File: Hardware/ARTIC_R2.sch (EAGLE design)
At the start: 103 parts, among them J1 U.FL, J2 THING_PLUS, Q1 20V/4.2A/52mΩ/1.4W, U1 32M SPI Flash, U2 1.8V/100mA, U3 ARTIC_R2, U4 RFPA0133, U5 AS179-92LF, U6 DUAL-OPTOISOLATOR_SOIC8, X1 CRYSTAL-TCXO-26MHZ

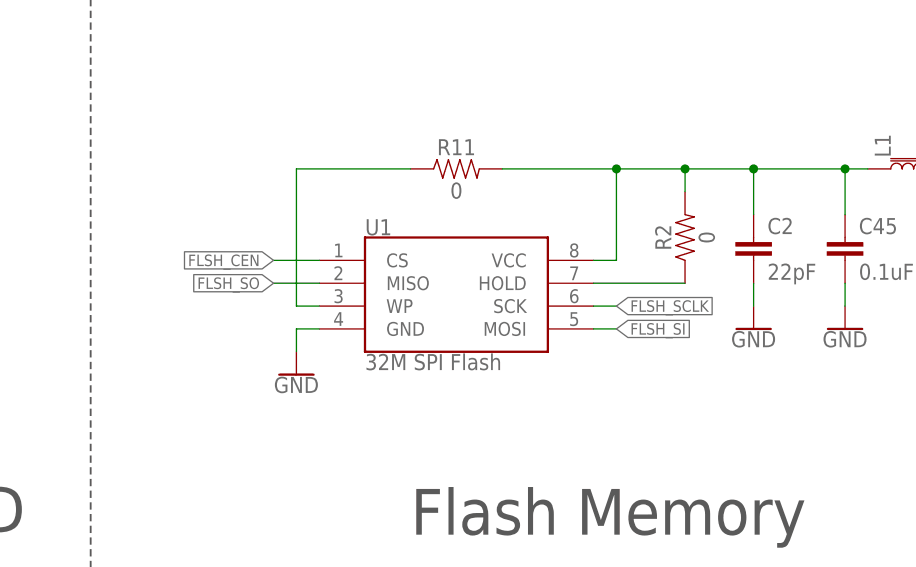
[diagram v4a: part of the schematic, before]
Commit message: Updated the flash memory
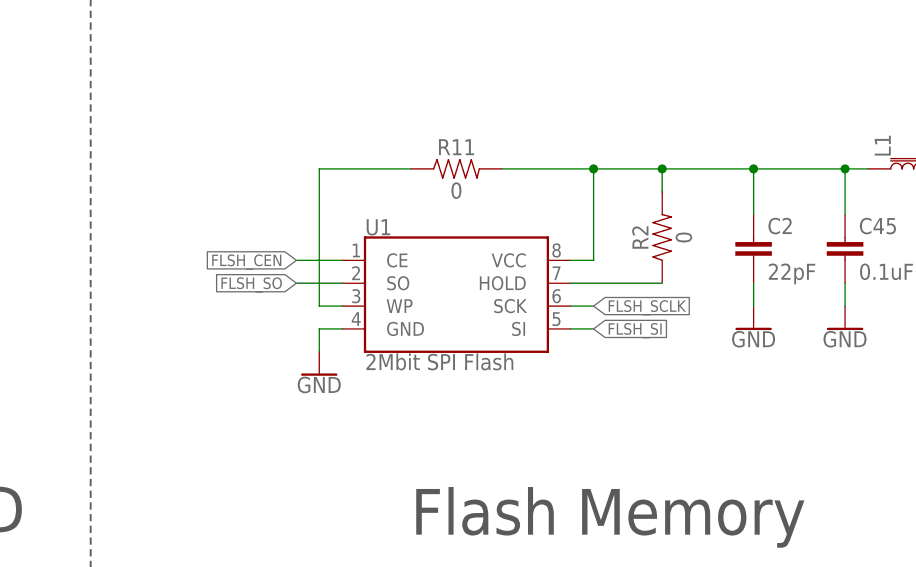
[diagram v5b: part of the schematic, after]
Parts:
- U1: value 32M SPI Flash -> 2Mbit SPI Flash; device SparkFun-IC-Memory:SPI_FLASH-X25XXSMD -> New_Parts_IC-Memory:SST25VF020BSMD
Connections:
- net FLSH_CEN: now also U1.CE; no longer U1.CS
- net FLSH_SI: now also U1.SI; no longer U1.MOSI
- net FLSH_SO: now also U1.SO; no longer U1.MISO
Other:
- moved on the sheet: R2
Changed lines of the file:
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@@
 <part name="R1" library="SparkFun-Resistors" deviceset="100KOHM" device="-0402T-1/16W-1%" value="100k"/>
 <part name="SUPPLY3" library="SparkFun-PowerSymbols" deviceset="VDD" device=""/>
-<part name="U1" library="SparkFun-IC-Memory" deviceset="SPI_FLASH-X25XX" device="SMD" value="32M SPI Flash"/>
 <part name="C1" library="SparkFun-Capacitors" deviceset="10UF" device="-0402T-6.3V-20%" value="10uF"/>
 <part name="SUPPLY4" library="SparkFun-PowerSymbols" deviceset="3.3V" device=""/>
@@
 <part name="JP6" library="SparkFun-Jumpers" deviceset="JUMPER-SMT_2_NO" device="_SILK" package3d_urn="urn:adsk.eagle:package:39279/1"/>
 <part name="JP7" library="SparkFun-Jumpers" deviceset="JUMPER-SMT_2_NO" device="_SILK" package3d_urn="urn:adsk.eagle:package:39279/1"/>
+<part name="U1" library="New_Parts_IC-Memory" deviceset="SST25VF020B" device="SMD" value="2Mbit SPI Flash"/>
 </parts>
 <sheets>
@@
 <attribute name="VALUE" x="66.04" y="251.714" size="1.778" layer="96" align="bottom-center"/>
 </instance>
-<instance part="U1" gate="G$1" x="167.64" y="241.3" smashed="yes">
-<attribute name="NAME" x="157.48" y="246.634" size="1.778" layer="95" font="vector"/>
-<attribute name="VALUE" x="157.48" y="233.426" size="1.778" layer="96" font="vector" align="top-left"/>
-</instance>
 <instance part="C1" gate="G$1" x="22.86" y="241.3" smashed="yes">
 <attribute name="NAME" x="24.384" y="244.221" size="1.778" layer="95" font="vector"/>
@@
 <attribute name="VALUE" x="212.344" y="241.681" size="1.778" layer="96" font="vector"/>
 </instance>
-<instance part="GND3" gate="1" x="149.86" y="231.14" smashed="yes">
-<attribute name="VALUE" x="149.86" y="230.886" size="1.778" layer="96" font="vector" align="top-center"/>
-</instance>
-<instance part="R2" gate="G$1" x="193.04" y="246.38" smashed="yes" rot="R90">
-<attribute name="NAME" x="191.516" y="246.38" size="1.778" layer="95" font="vector" rot="R90" align="bottom-center"/>
-<attribute name="VALUE" x="194.564" y="246.38" size="1.778" layer="96" font="vector" rot="R90" align="top-center"/>
+<instance part="GND3" gate="1" x="152.4" y="231.14" smashed="yes">
+<attribute name="VALUE" x="152.4" y="230.886" size="1.778" layer="96" font="vector" align="top-center"/>
+</instance>
+<instance part="R2" gate="G$1" x="190.5" y="246.38" smashed="yes" rot="R90">
+<attribute name="NAME" x="188.976" y="246.38" size="1.778" layer="95" font="vector" rot="R90" align="bottom-center"/>
+<attribute name="VALUE" x="192.024" y="246.38" size="1.778" layer="96" font="vector" rot="R90" align="top-center"/>
 </instance>
 <instance part="R11" gate="G$1" x="167.64" y="254" smashed="yes">
@@
 <instance part="JP7" gate="G$1" x="53.34" y="172.72" smashed="yes">
 <attribute name="NAME" x="50.8" y="175.26" size="1.778" layer="95" font="vector"/>
+</instance>
+<instance part="U1" gate="G$1" x="167.64" y="241.3" smashed="yes">
+<attribute name="NAME" x="157.48" y="246.634" size="1.778" layer="95" font="vector"/>
+<attribute name="VALUE" x="157.48" y="233.426" size="1.778" layer="96" font="vector" align="top-left"/>
 </instance>
 </instances>
@@
 </segment>
 <segment>
+<pinref part="GND3" gate="1" pin="GND"/>
+<wire x1="152.4" y1="236.22" x2="152.4" y2="233.68" width="0.1524" layer="91"/>
 <pinref part="U1" gate="G$1" pin="GND"/>
-<wire x1="152.4" y1="236.22" x2="149.86" y2="236.22" width="0.1524" layer="91"/>
-<pinref part="GND3" gate="1" pin="GND"/>
-<wire x1="149.86" y1="236.22" x2="149.86" y2="233.68" width="0.1524" layer="91"/>
+<wire x1="154.94" y1="236.22" x2="152.4" y2="236.22" width="0.1524" layer="91"/>
 </segment>
 <segment>
@@
 </segment>
 <segment>
+<label x="182.88" y="238.76" size="1.27" layer="95" xref="yes"/>
 <pinref part="U1" gate="G$1" pin="SCK"/>
-<wire x1="182.88" y1="238.76" x2="185.42" y2="238.76" width="0.1524" layer="91"/>
-<label x="185.42" y="238.76" size="1.27" layer="95" xref="yes"/>
+<wire x1="180.34" y1="238.76" x2="182.88" y2="238.76" width="0.1524" layer="91"/>
 </segment>
 </net>
@@
 </segment>
 <segment>
-<pinref part="U1" gate="G$1" pin="MOSI"/>
-<wire x1="182.88" y1="236.22" x2="185.42" y2="236.22" width="0.1524" layer="91"/>
-<label x="185.42" y="236.22" size="1.27" layer="95" xref="yes"/>
+<label x="182.88" y="236.22" size="1.27" layer="95" xref="yes"/>
+<pinref part="U1" gate="G$1" pin="SI"/>
+<wire x1="180.34" y1="236.22" x2="182.88" y2="236.22" width="0.1524" layer="91"/>
 </segment>
 </net>
@@
 </segment>
 <segment>
-<pinref part="U1" gate="G$1" pin="MISO"/>
-<wire x1="152.4" y1="241.3" x2="147.32" y2="241.3" width="0.1524" layer="91"/>
-<label x="147.32" y="241.3" size="1.27" layer="95" rot="R180" xref="yes"/>
+<label x="149.86" y="241.3" size="1.27" layer="95" rot="R180" xref="yes"/>
+<pinref part="U1" gate="G$1" pin="SO"/>
+<wire x1="154.94" y1="241.3" x2="149.86" y2="241.3" width="0.1524" layer="91"/>
 </segment>
 </net>
@@
 </segment>
 <segment>
-<pinref part="U1" gate="G$1" pin="CS"/>
-<wire x1="152.4" y1="243.84" x2="147.32" y2="243.84" width="0.1524" layer="91"/>
-<label x="147.32" y="243.84" size="1.27" layer="95" rot="R180" xref="yes"/>
+<label x="149.86" y="243.84" size="1.27" layer="95" rot="R180" xref="yes"/>
+<pinref part="U1" gate="G$1" pin="CE"/>
+<wire x1="154.94" y1="243.84" x2="149.86" y2="243.84" width="0.1524" layer="91"/>
 </segment>
 </net>
@@
 <pinref part="L1" gate="G$1" pin="1"/>
 <wire x1="200.66" y1="254" x2="210.82" y2="254" width="0.1524" layer="91"/>
-<pinref part="U1" gate="G$1" pin="VCC"/>
 <wire x1="210.82" y1="254" x2="213.36" y2="254" width="0.1524" layer="91"/>
-<wire x1="182.88" y1="243.84" x2="185.42" y2="243.84" width="0.1524" layer="91"/>
-<wire x1="185.42" y1="243.84" x2="185.42" y2="254" width="0.1524" layer="91"/>
-<wire x1="185.42" y1="254" x2="193.04" y2="254" width="0.1524" layer="91"/>
+<wire x1="182.88" y1="254" x2="190.5" y2="254" width="0.1524" layer="91"/>
 <junction x="200.66" y="254"/>
 <pinref part="R2" gate="G$1" pin="2"/>
-<wire x1="193.04" y1="254" x2="200.66" y2="254" width="0.1524" layer="91"/>
-<wire x1="193.04" y1="251.46" x2="193.04" y2="254" width="0.1524" layer="91"/>
-<junction x="193.04" y="254"/>
+<wire x1="190.5" y1="254" x2="200.66" y2="254" width="0.1524" layer="91"/>
+<wire x1="190.5" y1="251.46" x2="190.5" y2="254" width="0.1524" layer="91"/>
+<junction x="190.5" y="254"/>
 <pinref part="R11" gate="G$1" pin="2"/>
-<wire x1="172.72" y1="254" x2="185.42" y2="254" width="0.1524" layer="91"/>
-<junction x="185.42" y="254"/>
+<wire x1="172.72" y1="254" x2="182.88" y2="254" width="0.1524" layer="91"/>
+<junction x="182.88" y="254"/>
 <pinref part="C45" gate="G$1" pin="1"/>
 <wire x1="210.82" y1="248.92" x2="210.82" y2="254" width="0.1524" layer="91"/>
 <junction x="210.82" y="254"/>
+<pinref part="U1" gate="G$1" pin="VCC"/>
+<wire x1="180.34" y1="243.84" x2="182.88" y2="243.84" width="0.1524" layer="91"/>
+<wire x1="182.88" y1="243.84" x2="182.88" y2="254" width="0.1524" layer="91"/>
 </segment>
 </net>
 <net name="N$2" class="0">
 <segment>
+<pinref part="R2" gate="G$1" pin="1"/>
 <pinref part="U1" gate="G$1" pin="HOLD"/>
-<pinref part="R2" gate="G$1" pin="1"/>
-<wire x1="182.88" y1="241.3" x2="193.04" y2="241.3" width="0.1524" layer="91"/>
+<wire x1="180.34" y1="241.3" x2="190.5" y2="241.3" width="0.1524" layer="91"/>
 </segment>
 </net>
 <net name="N$3" class="0">
 <segment>
+<wire x1="152.4" y1="238.76" x2="152.4" y2="254" width="0.1524" layer="91"/>
+<pinref part="R11" gate="G$1" pin="1"/>
+<wire x1="152.4" y1="254" x2="162.56" y2="254" width="0.1524" layer="91"/>
 <pinref part="U1" gate="G$1" pin="WP"/>
-<wire x1="152.4" y1="238.76" x2="149.86" y2="238.76" width="0.1524" layer="91"/>
-<wire x1="149.86" y1="238.76" x2="149.86" y2="254" width="0.1524" layer="91"/>
-<pinref part="R11" gate="G$1" pin="1"/>
-<wire x1="149.86" y1="254" x2="162.56" y2="254" width="0.1524" layer="91"/>
-</segment>
-</net>
+<wire x1="154.94" y1="238.76" x2="152.4" y2="238.76" width="0.1524" layer="91"/>
+</segment>
+</net>
